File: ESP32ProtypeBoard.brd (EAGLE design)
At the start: 54.6 x 53.3 mm, 102 parts, among them IC1 ACT4088US-T, IC2 SI4431BDY, J1 CONN_03_NO_SILK, J2 CONN_04_NO_SILK, J20 CONN_04_NO_SILK, J21 CONN_05_NO_SILK, J24 CONN_04_NO_SILK, J31 CONN_01_NO_SILK, J38 CONN_01_NO_SILK, J4 VCC_TERMINAL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

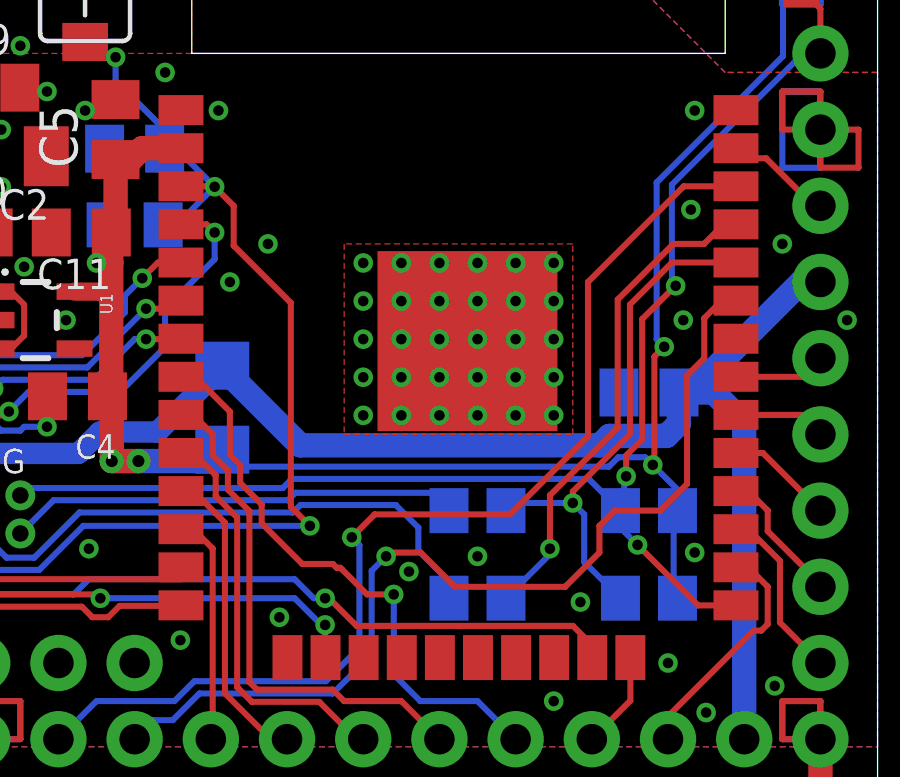
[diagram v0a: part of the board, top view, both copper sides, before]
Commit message: New ESP-WROOM-32D/E layout
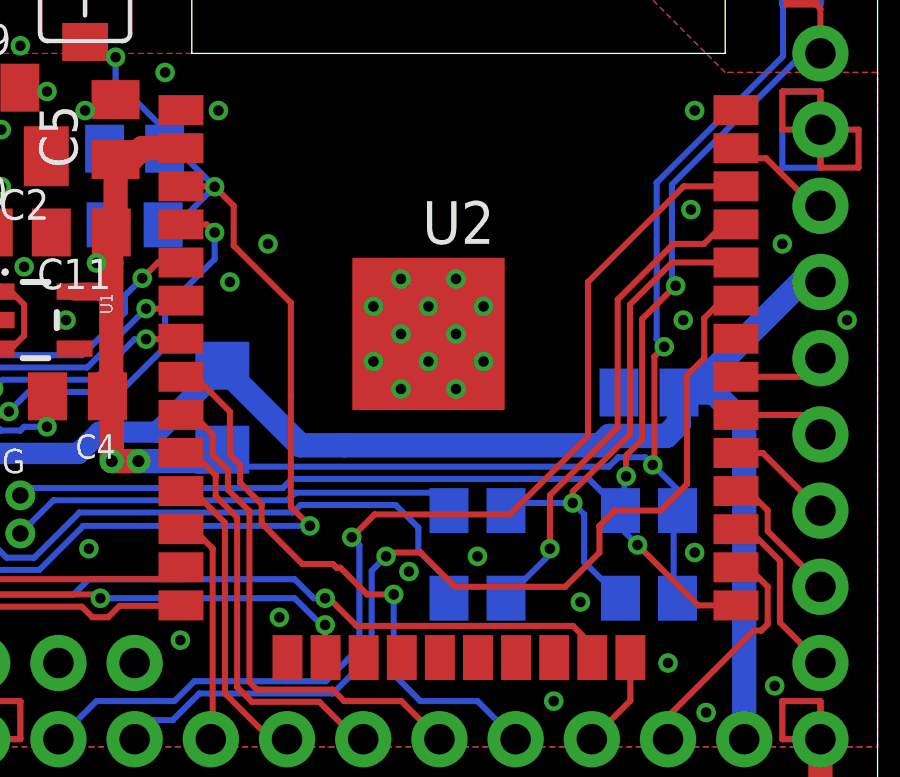
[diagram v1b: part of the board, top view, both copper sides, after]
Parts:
- U2: value ESP-WROOM-32 -> ESP-WROOM-32D; device esp32:ESP-WROOM-32 -> esp32-modified:ESP-WROOM-32D
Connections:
- net GND: now also U2.GND_1, U2.GND_10, U2.GND_11, U2.GND_12, U2.GND_2, U2.GND_3, U2.GND_4, U2.GND_5, U2.GND_6, U2.GND_7, U2.GND_8, U2.GND_9
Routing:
- net GND: vias 85 -> 55
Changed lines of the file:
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@@
 <drawing>
 <settings>
-<setting alwaysvectorfont="yes"/>
+<setting alwaysvectorfont="no"/>
 <setting verticaltext="up"/>
 </settings>
 <grid distance="25" unitdist="mil" unit="mil" style="lines" multiple="1" display="yes" altdistance="5" altunitdist="mil" altunit="mil"/>
 <layers>
-<layer number="1" name="Top" color="4" fill="1" visible="no" active="yes"/>
+<layer number="1" name="Top" color="4" fill="1" visible="yes" active="yes"/>
 <layer number="2" name="Route2" color="1" fill="3" visible="no" active="yes"/>
 <layer number="3" name="Route3" color="4" fill="3" visible="no" active="yes"/>
@@
 <layer number="19" name="Unrouted" color="6" fill="1" visible="yes" active="yes"/>
 <layer number="20" name="Dimension" color="24" fill="1" visible="yes" active="yes"/>
-<layer number="21" name="tPlace" color="7" fill="1" visible="no" active="yes"/>
+<layer number="21" name="tPlace" color="7" fill="1" visible="yes" active="yes"/>
 <layer number="22" name="bPlace" color="7" fill="1" visible="yes" active="yes"/>
-<layer number="23" name="tOrigins" color="15" fill="1" visible="no" active="yes"/>
+<layer number="23" name="tOrigins" color="15" fill="1" visible="yes" active="yes"/>
 <layer number="24" name="bOrigins" color="15" fill="1" visible="yes" active="yes"/>
 <layer number="25" name="tNames" color="7" fill="1" visible="no" active="yes"/>
 <layer number="26" name="bNames" color="7" fill="1" visible="no" active="yes"/>
-<layer number="27" name="tValues" color="7" fill="1" visible="no" active="yes"/>
+<layer number="27" name="tValues" color="7" fill="1" visible="yes" active="yes"/>
 <layer number="28" name="bValues" color="7" fill="1" visible="yes" active="yes"/>
 <layer number="29" name="tStop" color="7" fill="3" visible="no" active="yes"/>
@@
 <layer number="37" name="tTest" color="7" fill="1" visible="no" active="yes"/>
 <layer number="38" name="bTest" color="7" fill="1" visible="no" active="yes"/>
-<layer number="39" name="tKeepout" color="4" fill="11" visible="no" active="yes"/>
+<layer number="39" name="tKeepout" color="4" fill="11" visible="yes" active="yes"/>
 <layer number="40" name="bKeepout" color="1" fill="11" visible="yes" active="yes"/>
-<layer number="41" name="tRestrict" color="4" fill="10" visible="no" active="yes"/>
+<layer number="41" name="tRestrict" color="4" fill="10" visible="yes" active="yes"/>
 <layer number="42" name="bRestrict" color="1" fill="10" visible="yes" active="yes"/>
 <layer number="43" name="vRestrict" color="2" fill="10" visible="no" active="yes"/>
@@
 <layer number="49" name="Reference" color="7" fill="1" visible="no" active="yes"/>
 <layer number="50" name="dxf" color="7" fill="1" visible="no" active="no"/>
-<layer number="51" name="tDocu" color="7" fill="1" visible="no" active="yes"/>
+<layer number="51" name="tDocu" color="7" fill="1" visible="yes" active="yes"/>
 <layer number="52" name="bDocu" color="7" fill="1" visible="yes" active="yes"/>
 <layer number="53" name="tGND_GNDA" color="7" fill="9" visible="no" active="no"/>
@@
 </autorouter>
 <elements>
-<element name="U2" library="esp32" package="ESP-WROOM-32" value="ESP-WROOM-32" x="40.64" y="38.735" smashed="yes">
-<attribute name="VALUE" x="40.64" y="41.91" size="1.27" layer="27" font="vector" ratio="12" align="bottom-center"/>
+<element name="U2" library="esp32-modified" package="ESP-WROOM-32D" value="ESP-WROOM-32D" x="40.64" y="38.735" locked="yes" smashed="yes">
+<attribute name="NAME" x="40.64" y="41.275" size="1.4224" layer="25" font="vector" ratio="12" align="bottom-center"/>
+<attribute name="VALUE" x="40.64" y="40.894" size="1.016" layer="27" font="vector" ratio="12" rot="R180" align="top-center"/>
 </element>
 <element name="C4" library="rcl" library_urn="urn:adsk.eagle:library:334" package="C0805K" package3d_urn="urn:adsk.eagle:package:23681/2" value="22uF" x="27.94" y="36.195" smashed="yes" rot="R180">
@@
 <contactref element="IC2" pad="4"/>
 <contactref element="D1" pad="C"/>
-<polygon width="0.1524" layer="1" thermals="no">
-<vertex x="36.83" y="41.275"/>
-<vertex x="36.83" y="34.925"/>
-<vertex x="44.45" y="34.925"/>
-<vertex x="44.45" y="41.275"/>
-</polygon>
 <contactref element="J_12V1" pad="1"/>
 <contactref element="J3" pad="1"/>
@@
 <contactref element="C11" pad="2"/>
 <contactref element="RESET" pad="1"/>
-<via x="37.465" y="40.64" extent="1-16" drill="0.35"/>
-<via x="37.465" y="36.83" extent="1-16" drill="0.35"/>
-<via x="37.465" y="35.56" extent="1-16" drill="0.35"/>
-<via x="38.735" y="40.64" extent="1-16" drill="0.35"/>
-<via x="37.465" y="38.1" extent="1-16" drill="0.35"/>
-<via x="37.465" y="39.37" extent="1-16" drill="0.35"/>
 <via x="48.514" y="45.72" extent="1-16" drill="0.35"/>
 <contactref element="U1" pad="2"/>
@@
 <via x="30.861" y="46.99" extent="1-16" drill="0.35"/>
 <via x="32.639" y="45.72" extent="1-16" drill="0.35"/>
-<via x="38.735" y="39.37" extent="1-16" drill="0.35"/>
 <via x="17.526" y="43.18" extent="1-16" drill="0.35"/>
 <via x="13.97" y="48.26" extent="1-16" drill="0.35"/>
@@
 <wire x1="3.175" y1="42.545" x2="3.27" y2="42.64" width="0.2032" layer="16"/>
 <wire x1="3.27" y1="42.64" x2="5.7634" y2="42.64" width="0.2032" layer="16"/>
-<via x="38.735" y="38.1" extent="1-16" drill="0.35"/>
-<via x="38.735" y="36.83" extent="1-16" drill="0.35"/>
-<via x="38.735" y="35.56" extent="1-16" drill="0.35"/>
-<via x="40.005" y="35.56" extent="1-16" drill="0.35"/>
-<via x="40.005" y="36.83" extent="1-16" drill="0.35"/>
-<via x="40.005" y="38.1" extent="1-16" drill="0.35"/>
-<via x="40.005" y="39.37" extent="1-16" drill="0.35"/>
-<via x="40.005" y="40.64" extent="1-16" drill="0.35"/>
-<via x="41.275" y="40.64" extent="1-16" drill="0.35"/>
-<via x="41.275" y="39.37" extent="1-16" drill="0.35"/>
-<via x="41.275" y="38.1" extent="1-16" drill="0.35"/>
-<via x="41.275" y="36.83" extent="1-16" drill="0.35"/>
-<via x="41.275" y="35.56" extent="1-16" drill="0.35"/>
-<via x="42.545" y="35.56" extent="1-16" drill="0.35"/>
-<via x="42.545" y="36.83" extent="1-16" drill="0.35"/>
-<via x="42.545" y="38.1" extent="1-16" drill="0.35"/>
-<via x="42.545" y="39.37" extent="1-16" drill="0.35"/>
-<via x="42.545" y="40.64" extent="1-16" drill="0.35"/>
 <wire x1="52.705" y1="24.765" x2="52.705" y2="22.225" width="0.8128" layer="1"/>
 <wire x1="52.705" y1="22.225" x2="52.705" y2="19.685" width="0.8128" layer="1"/>
@@
 <via x="48.387" y="42.418" extent="1-16" drill="0.35"/>
 <via x="5.715" y="36.83" extent="1-16" drill="0.35"/>
-<via x="43.815" y="40.64" extent="1-16" drill="0.35"/>
-<via x="43.815" y="39.37" extent="1-16" drill="0.35"/>
-<via x="43.815" y="38.1" extent="1-16" drill="0.35"/>
-<via x="43.815" y="36.83" extent="1-16" drill="0.35"/>
-<via x="43.815" y="35.56" extent="1-16" drill="0.35"/>
 <wire x1="26.924" y1="35.179" x2="26.162" y2="35.179" width="0.2032" layer="16"/>
 <wire x1="26.162" y1="35.179" x2="26.036" y2="35.053" width="0.2032" layer="16"/>
@@
 <wire x1="11.43" y1="44.45" x2="12.7" y2="44.45" width="0.2032" layer="1"/>
 <wire x1="12.7" y1="44.45" x2="12.7" y2="45.72" width="0.2032" layer="1"/>
+<contactref element="U2" pad="GND_1"/>
+<contactref element="U2" pad="GND_2"/>
+<contactref element="U2" pad="GND_3"/>
+<contactref element="U2" pad="GND_4"/>
+<contactref element="U2" pad="GND_5"/>
+<contactref element="U2" pad="GND_6"/>
+<contactref element="U2" pad="GND_7"/>
+<contactref element="U2" pad="GND_8"/>
+<contactref element="U2" pad="GND_9"/>
+<contactref element="U2" pad="GND_10"/>
+<contactref element="U2" pad="GND_11"/>
+<contactref element="U2" pad="GND_12"/>
 </signal>
 <signal name="+3V3">
@@
 <wire x1="33.146" y1="41.2176" x2="33.146" y2="42.546" width="0.2032" layer="1"/>
 <wire x1="33.146" y1="42.546" x2="32.512" y2="43.18" width="0.2032" layer="1"/>
-<wire x1="35.052" y1="39.3116" x2="35.052" y2="32.512" width="0.2032" layer="1"/>
+<wire x1="35.052" y1="39.3116" x2="35.052" y2="36.195" width="0.2032" layer="1"/>
+<wire x1="35.052" y1="36.195" x2="35.052" y2="32.512" width="0.2032" layer="1"/>
 <wire x1="35.687" y1="31.877" x2="35.052" y2="32.512" width="0.2032" layer="1"/>
 <wire x1="35.052" y1="39.3116" x2="33.146" y2="41.2176" width="0.2032" layer="1"/>
 <wire x1="32.512" y1="43.18" x2="31.242" y2="44.45" width="0.2032" layer="16"/>
 <wire x1="31.242" y1="44.45" x2="30.845" y2="44.45" width="0.2032" layer="16"/>
+<wire x1="35.052" y1="36.195" x2="35.052" y2="36.195" width="0.2032" layer="1"/>
 </signal>
 <signal name="IO0">
@@
 <wire x1="34.0794" y1="32.5956" x2="34.0794" y2="31.9606" width="0.2032" layer="1"/>
 <wire x1="37.592" y1="29.591" x2="38.481" y2="29.591" width="0.2032" layer="1"/>
-<wire x1="36.703" y1="30.48" x2="36.7665" y2="30.4165" width="0.2032" layer="1"/>
-<wire x1="36.7665" y1="30.4165" x2="37.592" y2="29.591" width="0.2032" layer="1"/>
+<wire x1="36.703" y1="30.48" x2="37.592" y2="29.591" width="0.2032" layer="1"/>
 <wire x1="33.3627" y1="33.3123" x2="34.0794" y2="32.5956" width="0.2032" layer="1"/>
 <wire x1="41.275" y1="26.035" x2="42.545" y2="24.765" width="0.2032" layer="16"/>
@@
 <wire x1="32.766" y1="37.16680625" x2="30.60219375" y2="35.003" width="0.7112" layer="16"/>
 <wire x1="45.67005" y1="34.875" x2="45.35785" y2="34.5628" width="0.8128" layer="16"/>
-<wire x1="45.35785" y1="34.5628" x2="35.3644" y2="34.5628" width="0.8128" layer="16"/>
+<wire x1="45.35785" y1="34.5628" x2="36.83" y2="34.5628" width="0.8128" layer="16"/>
+<wire x1="36.83" y1="34.5628" x2="35.3644" y2="34.5628" width="0.8128" layer="16"/>
 <wire x1="32.766" y1="37.214" x2="32.766" y2="37.1612" width="0.8128" layer="16"/>
 <wire x1="35.3644" y1="34.5628" x2="32.766" y2="37.1612" width="0.8128" layer="16"/>

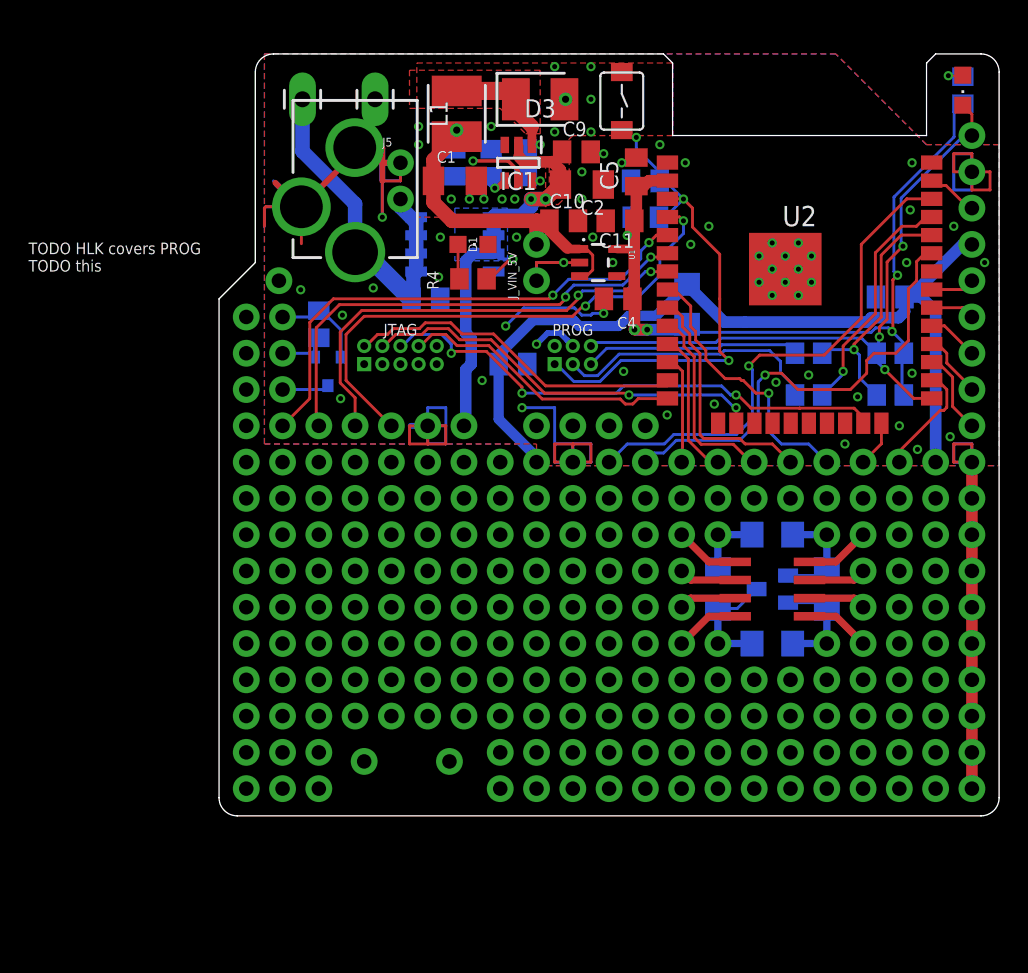
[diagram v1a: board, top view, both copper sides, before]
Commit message: Improved TPS562201DDCTT lbr, using it in design
WIP: Schematic only, no layout yet
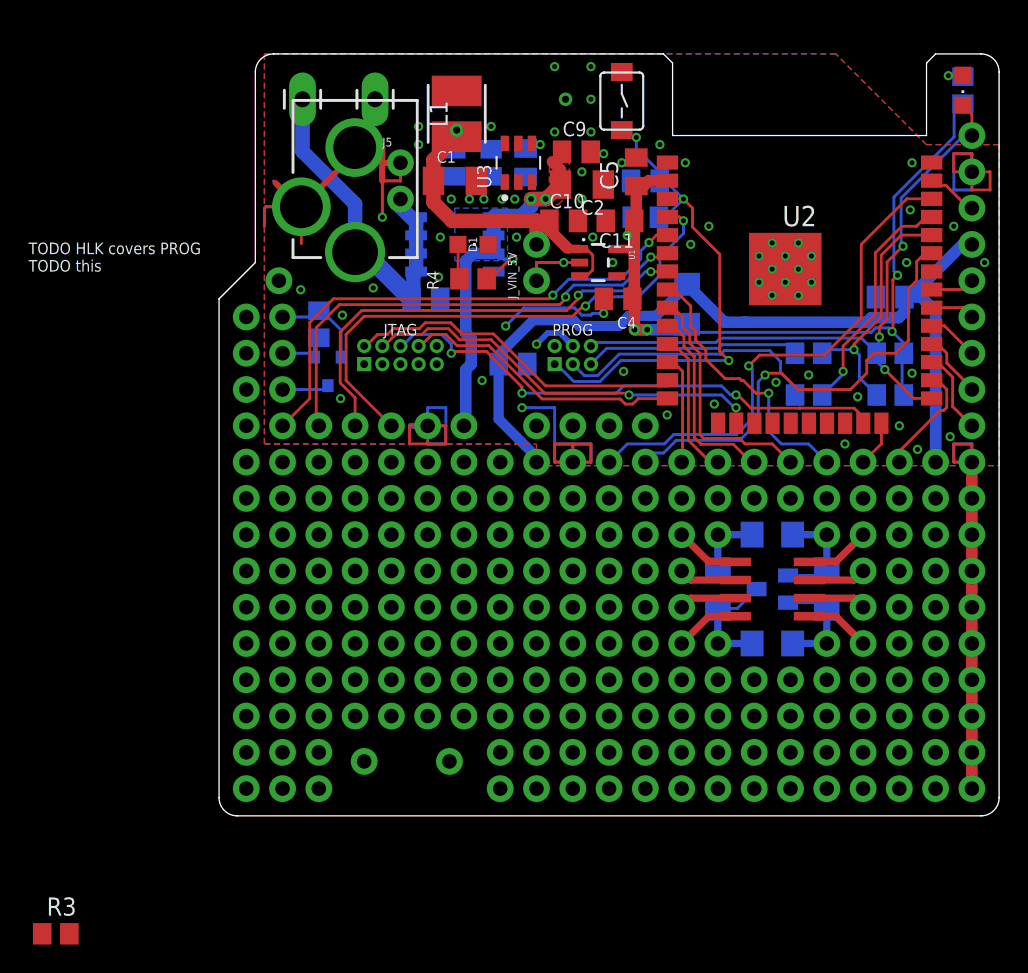
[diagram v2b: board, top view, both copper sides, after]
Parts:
- removed D3: B240AE-13, B240AE-13:DIOC4326X240N
- removed IC1: ACT4088US-T, ACT4088US-T:SOT95P280X145-6N
- added R3: 10K, rcl:R0805
- added U3: TPS562201DDCTTEXAS_INSTRUMENTS_TPS562201DDCT_0_0, TPS562201DDCT:TEXAS_INSTRUMENTS_TPS562201DDCT_0
- C7: value 22nF -> 0.1uF
- R12: value 150K -> 54.9K
- R13: value 28.7K -> 10K
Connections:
- removed net BST: C7.2, IC1.6
- new net N$12: C7.2, U3.6
- new net N$14: R3.2, U3.5
- net +12V: now also R3.1, U3.3; no longer IC1.2
- net FB: now also U3.4; no longer IC1.4
- net GND: now also U3.1; no longer D3.2, IC1.5
- net SW: now also U3.2; no longer D3.1, IC1.1
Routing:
- net SW: track 8.68 -> 1.16 mm
- net FB: track 4.39 -> 0.00 mm, vias 1 -> 0
- net GND: track 157.9 -> 153.8 mm, vias 55 -> 54
- net +12V: track 32.7 -> 29.3 mm
- net BST: track 1.71 -> 0.00 mm, vias 1 -> 0
- removed copper zone on layer 1, net SW
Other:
- board text added: "Mikee © 2021/05 v3.1"
- board text removed: "BA240"
- board text removed: "Mikee © 2021/05 v3"

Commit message: Removed restrict from TPS562201 lbr
WIP: converter layout
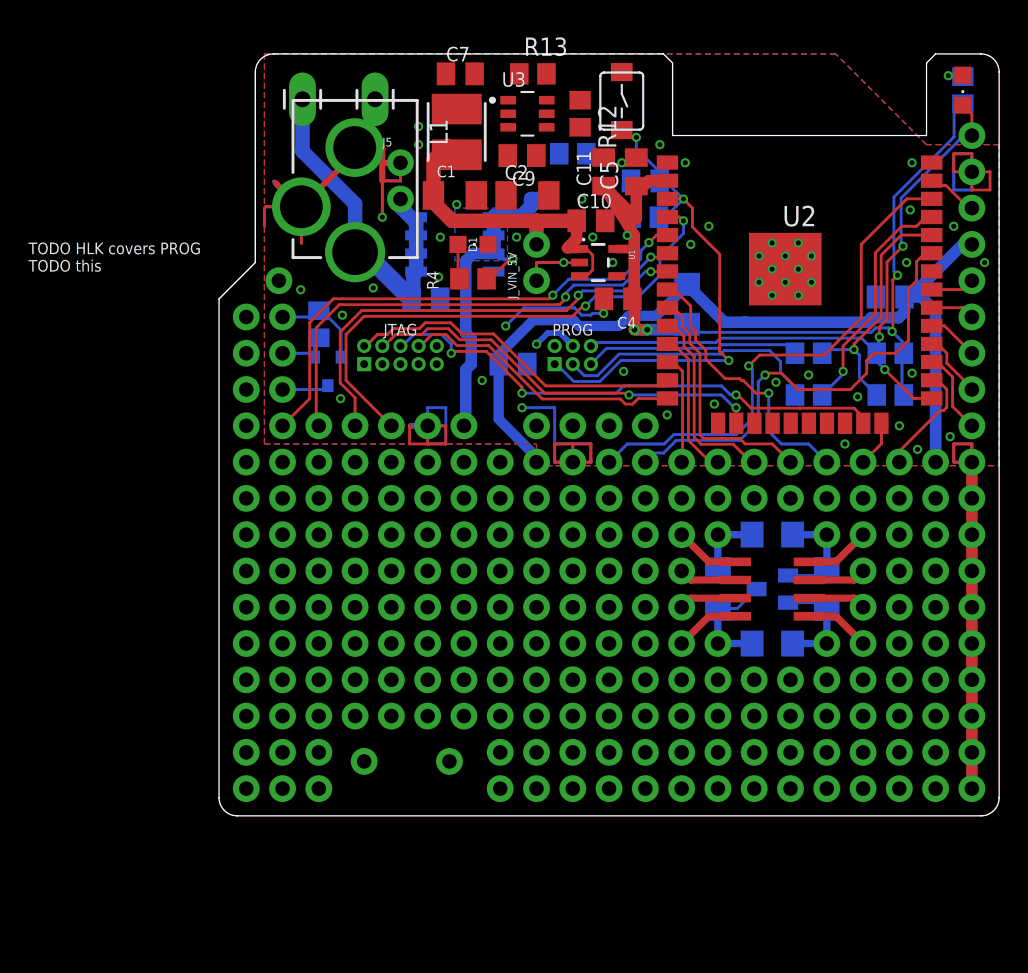
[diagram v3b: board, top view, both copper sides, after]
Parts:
- moved R3 65.5 mm to (24.8, 46.4), flipped to the bottom
- moved R12 9.41 mm to (25.3, 49.1), flipped to the top, turned to 270 degrees
- moved C7 7.72 mm to (16.9, 51.9), flipped to the top, turned to 0 degrees
- moved R13 6.87 mm to (22.0, 51.9), flipped to the top, turned to 0 degrees
- moved C2 3.89 mm to (21.6, 43.4), turned to 0 degrees
- moved C9 3.82 mm to (21.2, 46.2), turned to 180 degrees
- moved C11 3.61 mm to (26.9, 45.1), turned to 90 degrees
- moved U3 3.49 mm to (21.6, 49.1), turned to 0 degrees
- moved C10 1.91 mm to (26.0, 41.7)
- moved L1 1.27 mm to (16.6, 47.9)
- moved C1 1.02 mm to (16.5, 43.4)
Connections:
- net FB renamed VFB
- net N$12 renamed VBST
- net N$14 renamed VEN
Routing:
- net +3V3: track 58.5 -> 64.6 mm
- net +12V: track 29.3 -> 25.0 mm, vias 3 -> 1
- net SW: track 1.16 -> 0.00 mm, vias 1 -> 0
- net +5V: track 24.0 -> 24.2 mm, vias 1 -> 0
- net GND: vias 54 -> 41
- removed copper zone on layer 1, net +12V
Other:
- board text removed: "ACT4088"
